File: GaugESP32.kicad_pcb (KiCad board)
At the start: 2 copper layers, 63 parts, among them J1 Conn_01x20, J2 Conn_01x20, J3 JST-PH, J4 Conn_02x02_Counter_Clockwise, J5 Micro USB-B, Q1 MBT3946DW1T1, Q2 BC847, U1 ESP32PICO_D4, U2 FT231XS, U3 BQ24075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

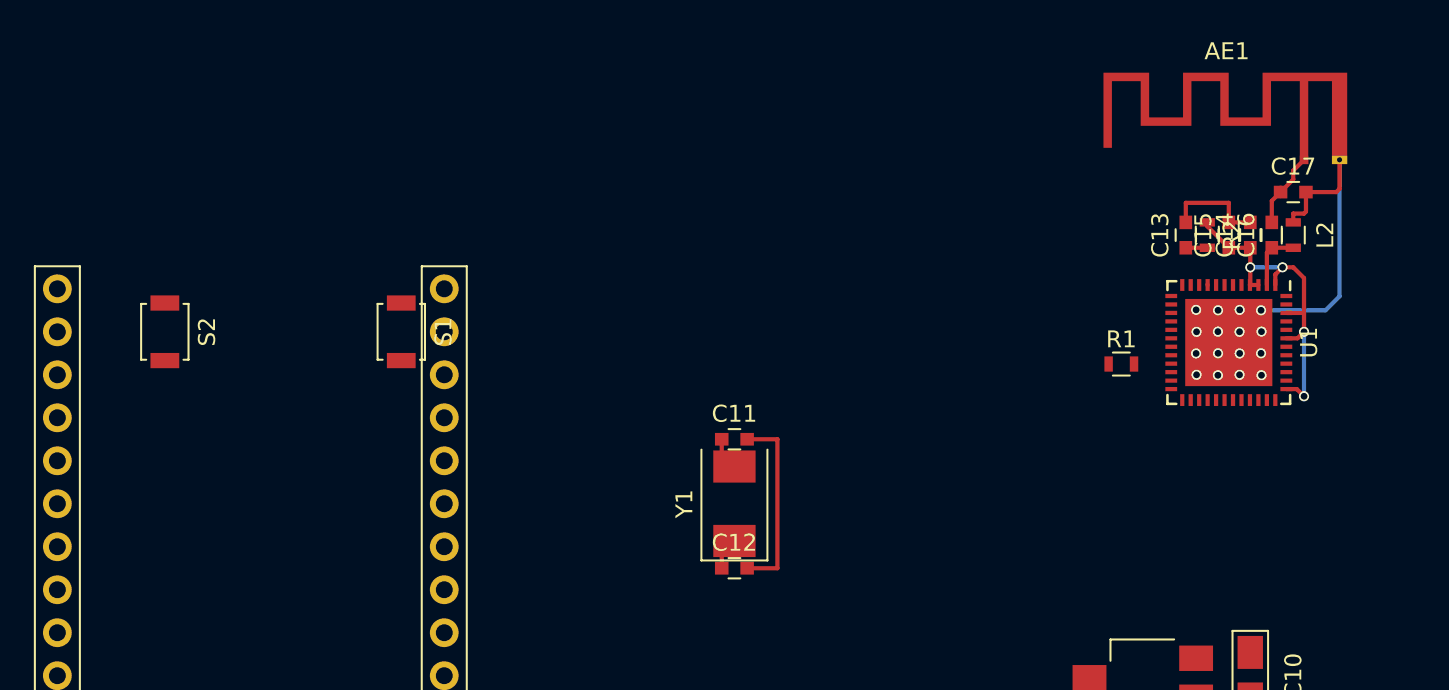
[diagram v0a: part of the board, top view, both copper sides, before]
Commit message: Main ESP32 components placement
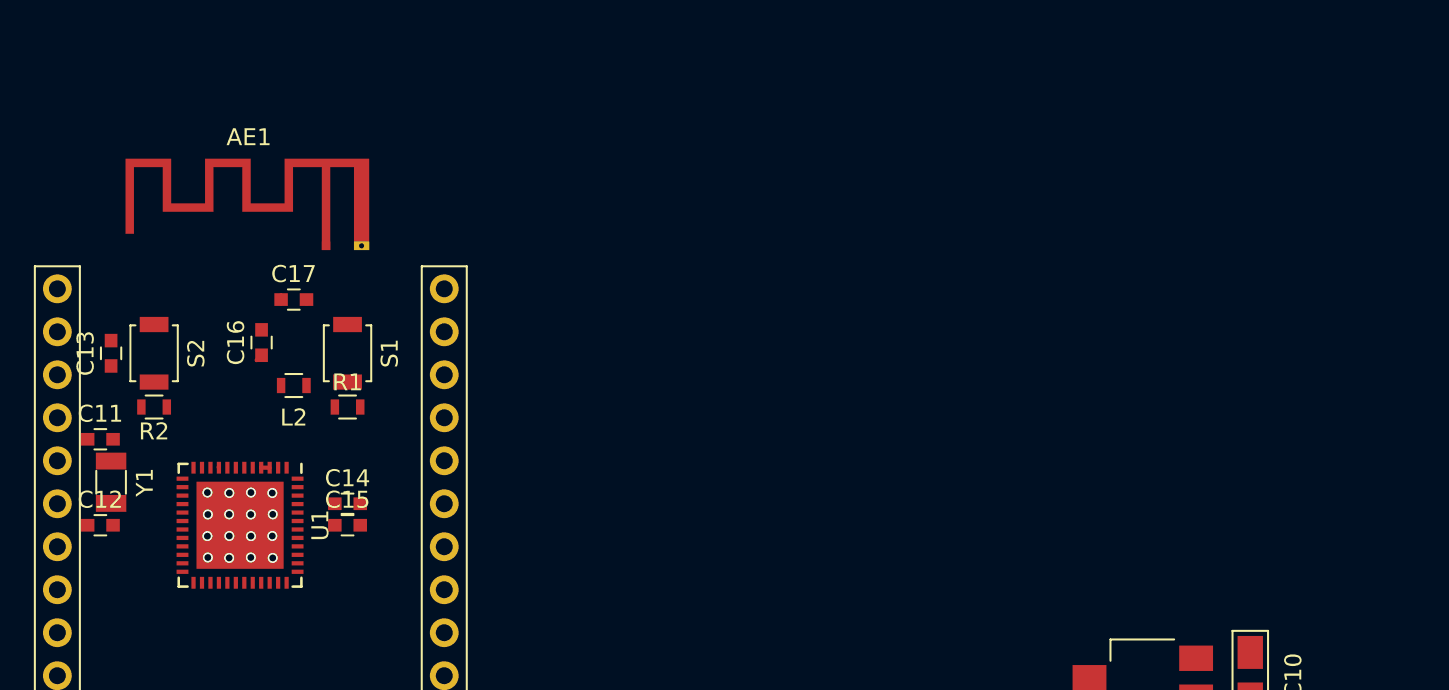
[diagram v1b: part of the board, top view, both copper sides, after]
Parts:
- Y1: footprint Crystals:Crystal_SMD_0603-2pin_6.0x3.5mm -> Crystals:Crystal_SMD_3215-2pin_3.2x1.5mm
- moved C13 63.9 mm to (85.1, 95.2)
- moved R2 63.1 mm to (87.6, 98.4), turned to 180 degrees
- moved C16 60.0 mm to (94.0, 94.6)
- moved L2 59.7 mm to (95.9, 97.2), turned to 180 degrees
- moved U1 59.4 mm to (92.7, 105.4)
- moved C17 59.4 mm to (95.9, 92.1)
- moved AE1 58.0 mm to (97.8, 88.9)
- moved C14 55.7 mm to (99.1, 104.1), turned to 0 degrees
- moved C15 54.8 mm to (99.1, 105.4), turned to 0 degrees
- moved R1 45.8 mm to (99.1, 98.4)
- moved C12 37.6 mm to (84.5, 105.4)
- moved C11 37.5 mm to (84.5, 100.3)
- moved Y1 36.9 mm to (85.1, 102.9), turned to 270 degrees
- moved S1 3.42 mm to (99.1, 95.2)
- moved S2 1.42 mm to (87.6, 95.2)
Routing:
- net GND: track 69.7 -> 33.0 mm
- net +3.3VA: track 21.4 -> 0.85 mm, vias 4 -> 0
- net Net-(AE1-Pad1): track 4.99 -> 0.51 mm
- net LNA: track 3.71 -> 0.53 mm
- net IO33: track 1.92 -> 0.00 mm
- net IO32: track 1.92 -> 0.00 mm
- net EN: track 1.30 -> 0.03 mm

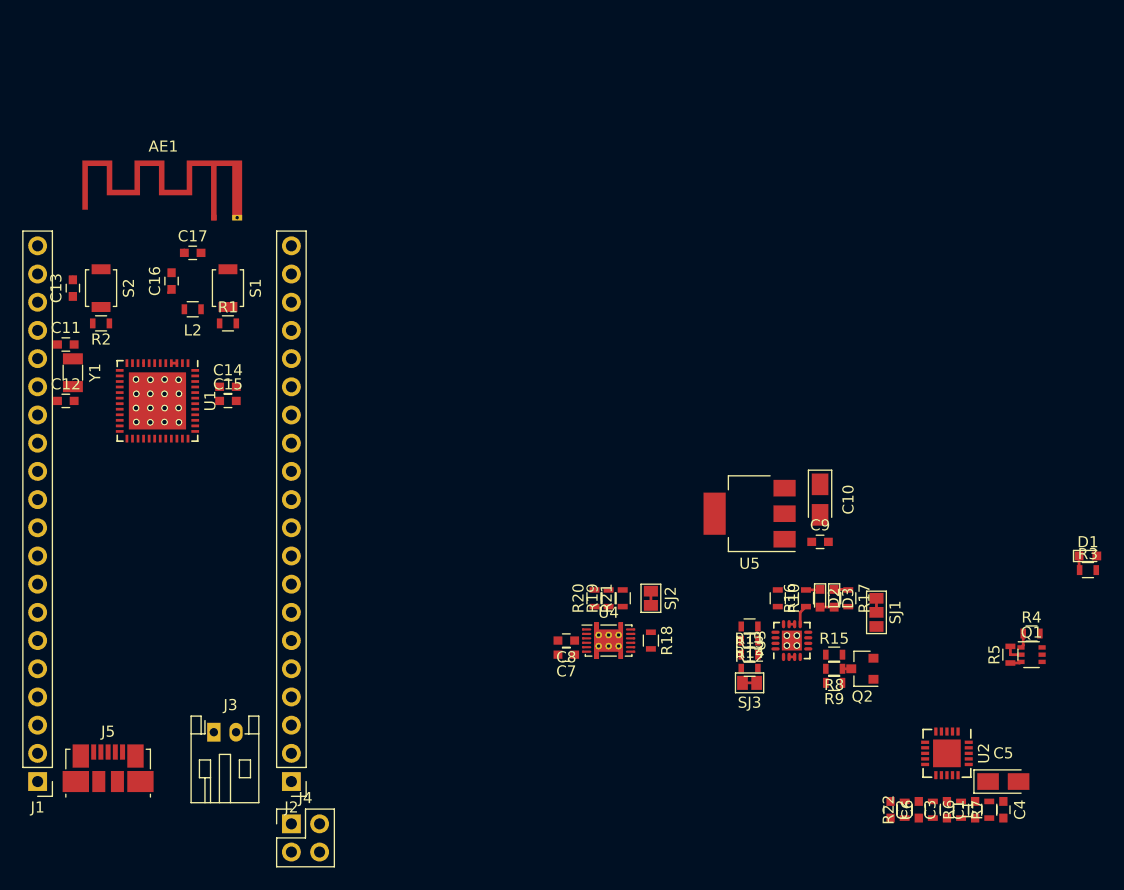
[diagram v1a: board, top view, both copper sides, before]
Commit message: Board layout placement
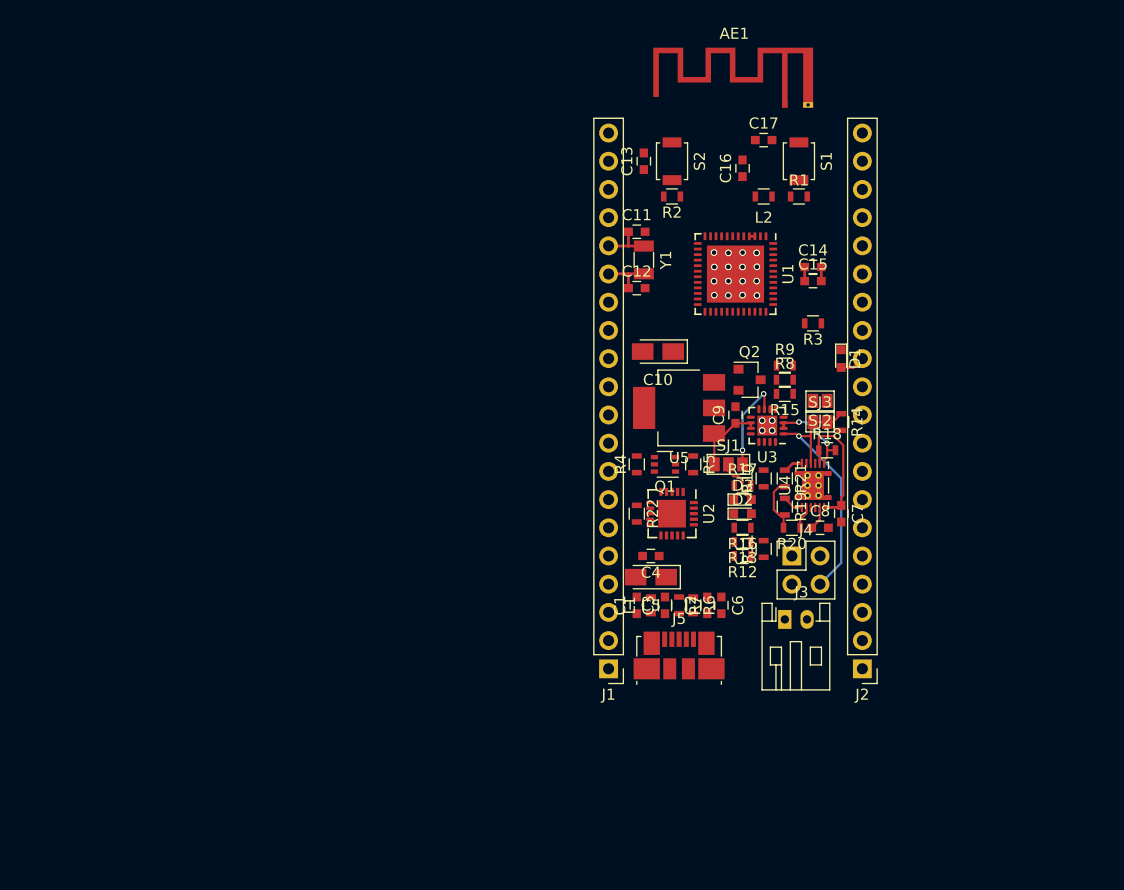
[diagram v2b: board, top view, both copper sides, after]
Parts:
- moved C14 53.8 mm to (151.8, 93.3)
- moved C15 53.8 mm to (151.8, 94.6)
- moved U1 53.3 mm to (144.8, 94.0)
- moved C13 52.7 mm to (136.5, 83.8)
- moved R1 52.7 mm to (150.5, 87.0)
- moved R2 52.7 mm to (139.1, 87.0)
- moved S1 52.7 mm to (150.5, 83.8)
- moved S2 52.7 mm to (139.1, 83.8)
- moved J2 52.4 mm to (156.2, 129.5)
- moved Y1 52.4 mm to (136.5, 92.7)
- moved AE1 52.4 mm to (149.2, 78.7)
- moved C11 52.4 mm to (135.9, 90.2)
- moved C12 52.4 mm to (135.9, 95.2)
- moved C16 52.4 mm to (145.4, 84.5)
- moved C17 52.4 mm to (147.3, 81.9)
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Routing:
- net TS: track 1.28 -> 25.5 mm, vias 0 -> 1
- net VBATT-RAW: track 0.00 -> 12.1 mm
- net Net-(SJ1-Pad1): track 0.00 -> 8.55 mm, vias 0 -> 2
- net +BATT: track 0.50 -> 7.94 mm, vias 0 -> 2
- net +3.3VA: track 0.85 -> 7.02 mm
- net IO33: track 0.00 -> 4.47 mm
- net IO32: track 0.00 -> 4.47 mm
- net Net-(D3-Pad2): track 0.00 -> 4.28 mm
- net VSYS: track 3.04 -> 7.00 mm
- net IO5: track 0.00 -> 2.24 mm
- net /1.8V: track 0.00 -> 2.13 mm
- net IO22: track 0.00 -> 2.06 mm
- net IO21: track 0.00 -> 1.88 mm
- net Net-(R16-Pad1): track 1.80 -> 0.00 mm
- net GPOUT: track 0.00 -> 1.79 mm
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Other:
- net class Default: clearance 0.2 -> 0.17; trace_width 0.25 -> 0.2; via_dia 0.6 -> 0.5; via_drill 0.4 -> 0.3
- rule trace_clearance: 0.2 -> 0.17

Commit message: Layout work
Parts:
- U2: footprint Housings_DFN_QFN:QFN-20-1EP_4x4mm_Pitch0.5mm -> Housings_SSOP:SSOP-20_5.3x7.2mm_Pitch0.65mm
- moved R22 20.7 mm to (151.8, 102.2), turned to 180 degrees
- moved C4 4.60 mm to (141.4, 121.3), turned to 0 degrees
- moved R14 4.10 mm to (150.5, 108.8)
- moved C14 3.07 mm to (150.2, 90.7)
- moved C15 2.96 mm to (150.2, 92.1)
- moved R5 2.07 mm to (140.6, 109.1)
- moved R4 2.04 mm to (136.0, 109.1)
- moved Q1 2.03 mm to (138.4, 109.1)
- moved R10 1.91 mm to (147.4, 110.5), turned to 180 degrees
- moved U5 1.91 mm to (139.6, 104.1)
- moved C10 1.78 mm to (137.8, 99.2)
- moved R20 1.53 mm to (148.7, 115.8)
- moved R13 1.52 mm to (145.4, 119.6)
- moved C7 1.40 mm to (154.2, 114.2), turned to 90 degrees
- moved R3 1.20 mm to (152.4, 99.4)
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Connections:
- U4 pad 13: (no net) -> GND
- U5 pad 4: (no net) -> GND
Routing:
- net GND: track 34.4 -> 316.3 mm, vias 20 -> 35
- net +3.3VA: track 7.02 -> 87.9 mm, vias 0 -> 8
- net IO0: track 0.00 -> 77.1 mm, vias 0 -> 2
- net RXD0: track 0.00 -> 55.2 mm, vias 0 -> 3
- net TXD0: track 0.00 -> 54.2 mm, vias 0 -> 3
- net EN: track 0.03 -> 47.6 mm, vias 0 -> 2
- net VBATT-RAW: track 12.1 -> 48.1 mm
- net IO15: track 0.00 -> 32.8 mm, vias 0 -> 4
- net IO16: track 0.00 -> 30.0 mm, vias 0 -> 2
- net VUSB-RAW: track 0.00 -> 27.8 mm, vias 0 -> 2
- net IO17: track 0.00 -> 26.0 mm, vias 0 -> 2
- net IO13: track 0.00 -> 25.0 mm
- net IO4: track 0.00 -> 24.3 mm, vias 0 -> 1
- net IO2: track 0.00 -> 23.9 mm, vias 0 -> 3
- net SLEEP#: track 0.00 -> 23.8 mm, vias 0 -> 2
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
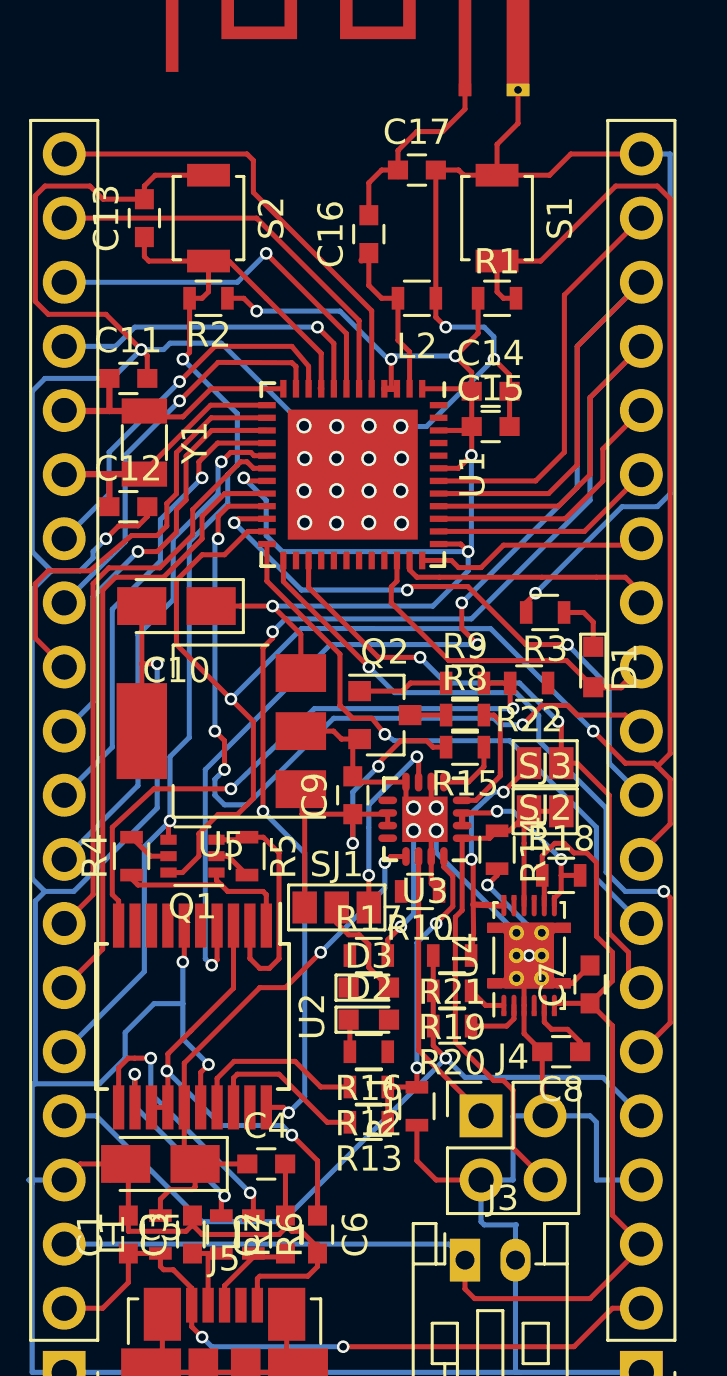
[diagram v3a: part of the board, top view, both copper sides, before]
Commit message: Layout trace complete
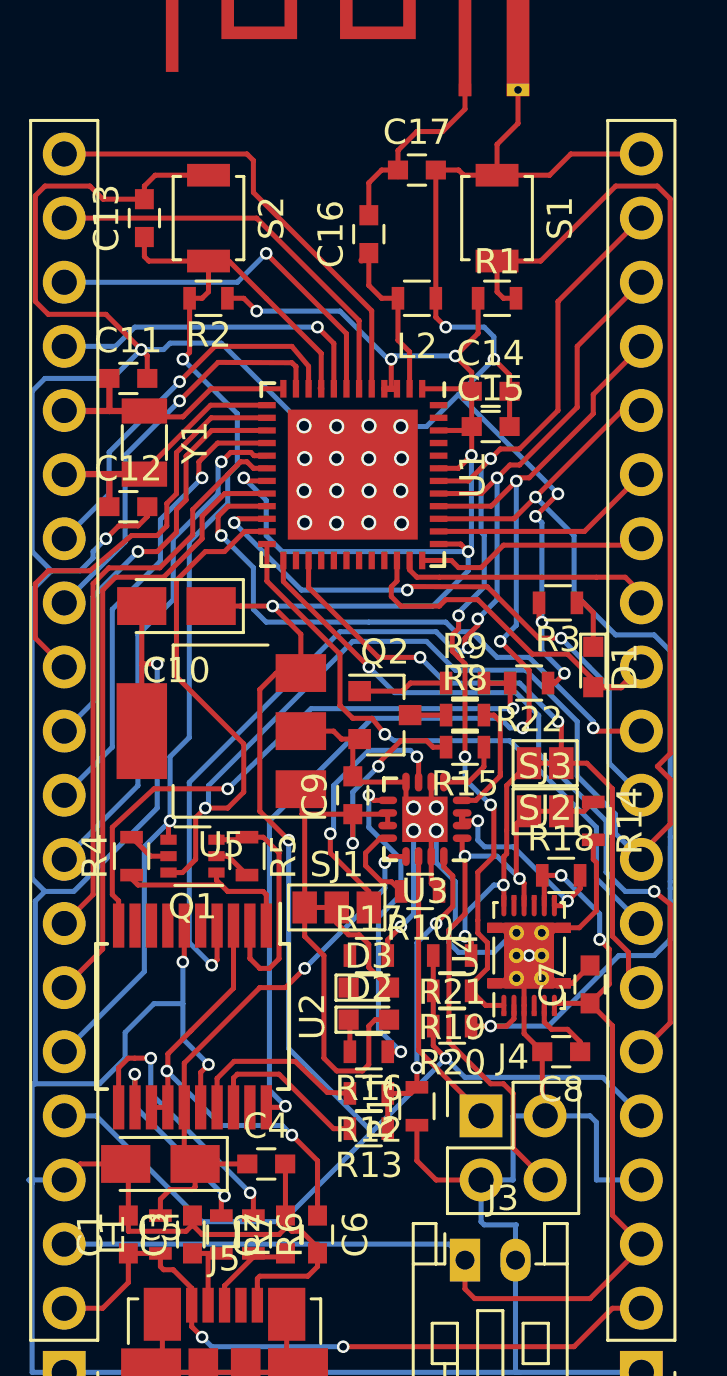
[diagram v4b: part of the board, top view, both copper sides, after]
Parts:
- moved R14 3.98 mm to (154.3, 107.7)
- moved R3 0.63 mm to (152.9, 99.1)
- moved R12 0.25 mm to (145.4, 118.5)
- moved R13 0.25 mm to (145.4, 119.9)
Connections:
- D3 pad 2: Net-(D3-Pad2) -> VSYS
- J2 pad 7: IO17 -> GPOUT
- SJ1 pad 2: Net-(D3-Pad2) -> VSYS
- SJ2 pad 1: IO17 -> GPOUT
- U1 pad 27: IO17 -> GPOUT
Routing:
- net IO22: track 13.5 -> 42.0 mm, vias 0 -> 2
- net GPOUT: track 10.2 -> 37.7 mm, vias 2 -> 4
- net IO17: track 26.0 -> 0.00 mm, vias 2 -> 0
- net IO21: track 17.5 -> 39.6 mm, vias 0 -> 4
- net +3.3VA: track 87.9 -> 109.2 mm, vias 8 -> 9
- net VSYS: track 16.5 -> 32.9 mm
- net Net-(R16-Pad1): track 0.00 -> 12.8 mm, vias 0 -> 2
- net TXD0: track 54.2 -> 43.4 mm, vias 3 -> 4
- net RXD0: track 55.2 -> 45.9 mm, vias 3 -> 4
- net IO15: track 32.8 -> 23.9 mm, vias 4 -> 2
- net IO0: track 77.1 -> 82.3 mm, vias 2 -> 1
- net Net-(D3-Pad2): track 4.28 -> 0.00 mm
- net GND: track 316.3 -> 312.6 mm, vias 35 -> 37
- net Net-(R10-Pad2): track 0.00 -> 3.45 mm
- net Net-(SJ1-Pad1): track 7.79 -> 10.5 mm
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
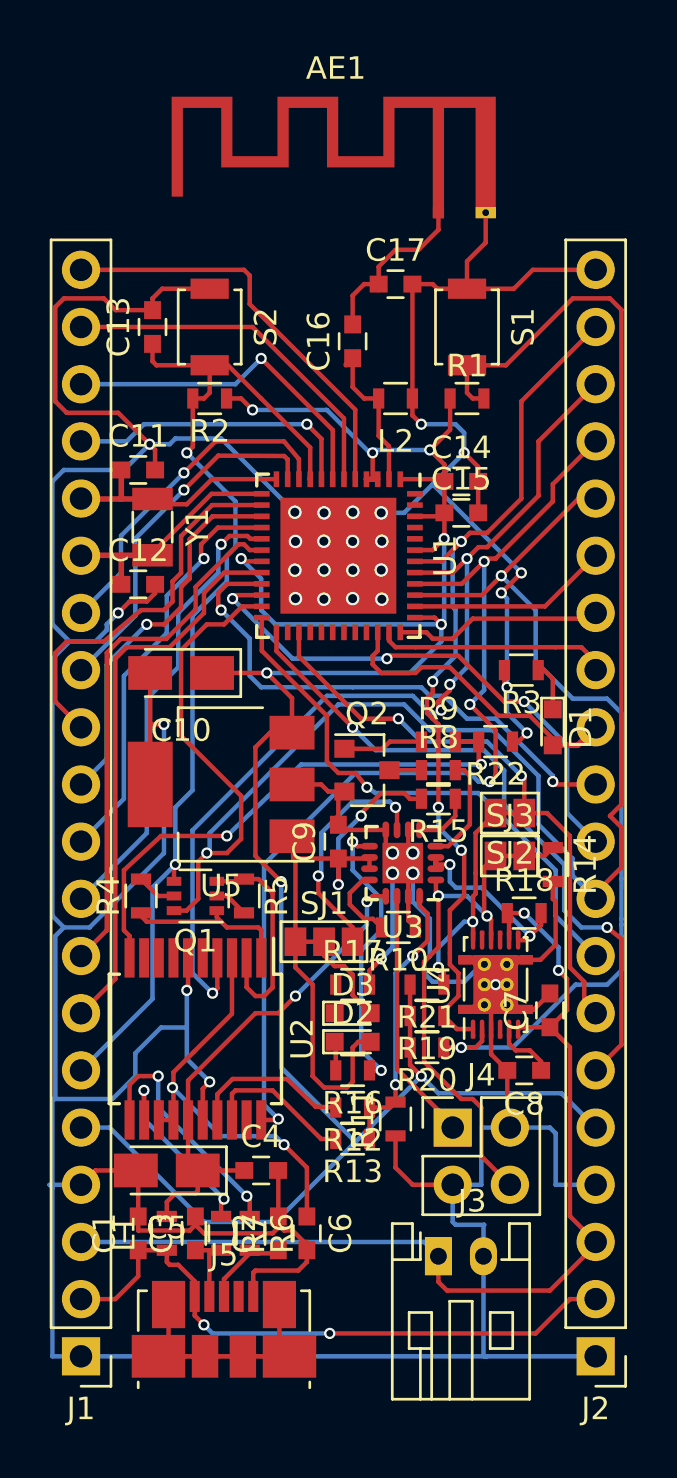
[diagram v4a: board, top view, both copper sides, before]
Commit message: Layout tracing and fill finalization
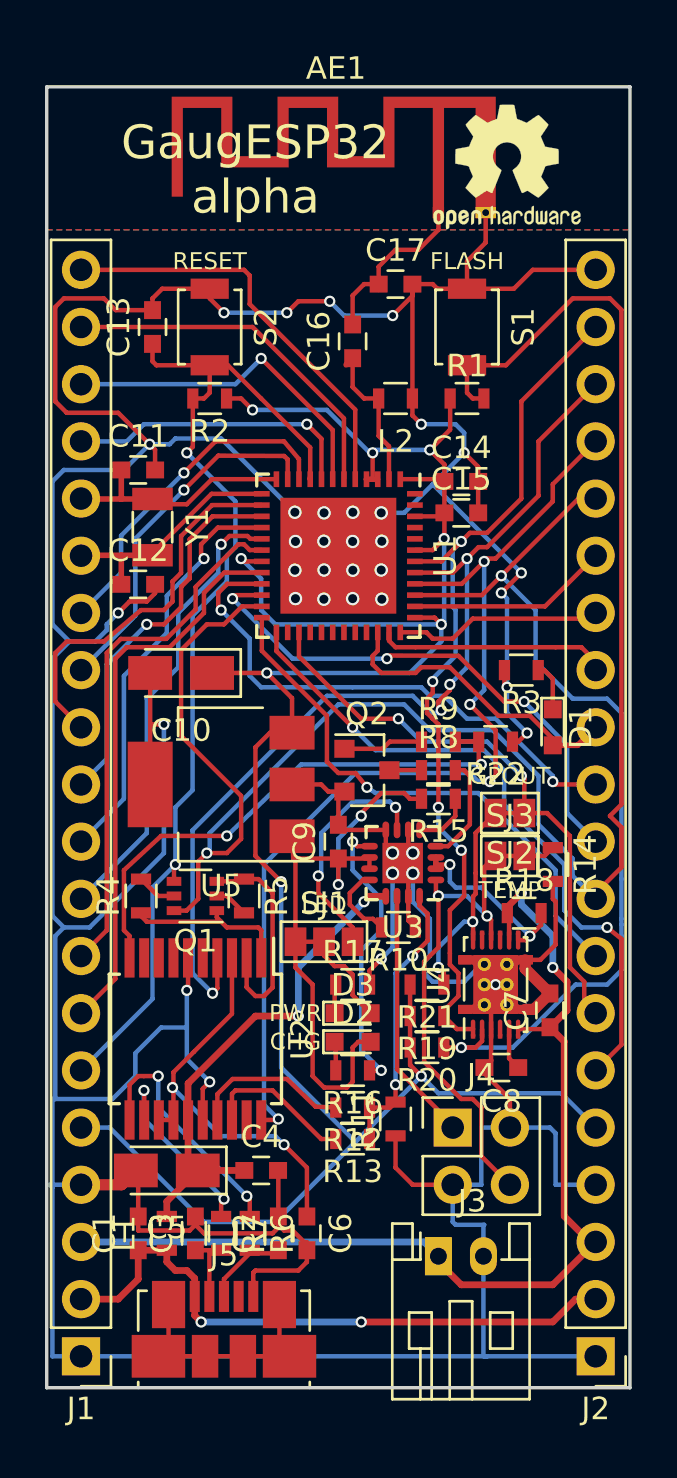
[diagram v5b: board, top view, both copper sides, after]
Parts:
- added REF***: OSHW-Logo2_7.3x6mm_SilkScreen, Symbols:OSHW-Logo2_7.3x6mm_SilkScreen, F.Cu at (152.3, 76.7)
- moved C8 1.02 mm to (152.0, 116.7)
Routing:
- net GND: track 312.6 -> 326.1 mm, vias 37 -> 41
- net Net-(D3-Pad1): track 0.07 -> 1.36 mm
- net VBATT-RAW: track 45.4 -> 46.3 mm
- net /1.8V: track 2.80 -> 1.88 mm
- net +5V: track 22.1 -> 22.8 mm
- added copper zone on B.Cu, net GND
- added copper zone on F.Cu, net GND
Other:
- board outline added: 25.9 x 57.8 mm
- net class 5V added: clearance 0.17, trace_width 0.3, via_dia 0.5, via_drill 0.3
- net class GND added: clearance 0.17, trace_width 0.5, via_dia 0.5, via_drill 0.3
- board text added: "CHG"
- board text added: "FLASH"
- board text added: "GPOUT"
- board text added: "GaugESP32 alpha"
- board text added: "LED"
- board text added: "PWR"
- board text added: "RESET"
- board text added: "TEMP"
